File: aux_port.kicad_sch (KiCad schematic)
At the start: 5 parts, among them J1 USB_C

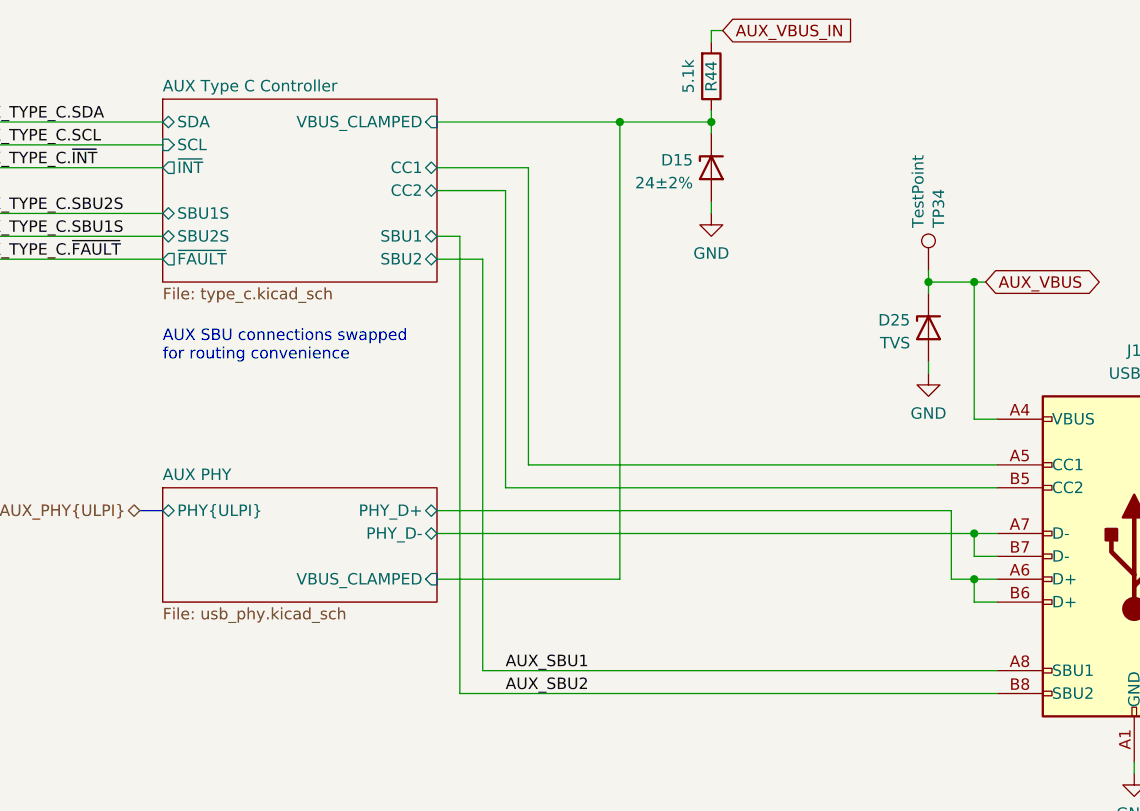
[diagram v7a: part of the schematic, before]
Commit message: Add second common-mode choke for TARGET port
Instead of having a single choke connected in series with the PHY, we
now have a choke in series with each connector. The PHY is connected
between the two chokes.
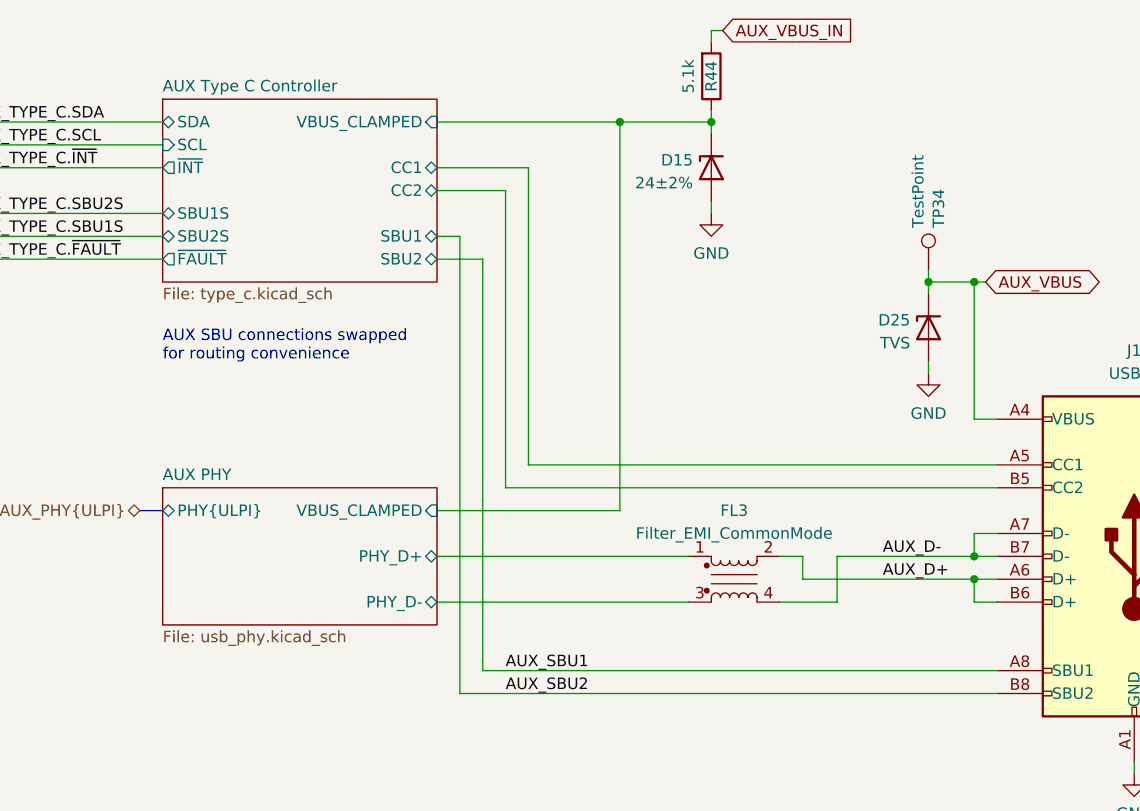
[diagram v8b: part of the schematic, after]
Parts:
- added FL3: Filter_EMI_CommonMode, cynthion:L_CommonModeChoke_Murata_DLM0NS, symbol Device:Filter_EMI_CommonMode
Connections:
- net AUX PHY/PHY_D+: now also FL3.1; no longer J1.A6 (D+), J1.B6 (D+)
- net AUX PHY/PHY_D-: now also FL3.3; no longer J1.A7 (D-), J1.B7 (D-)
- new net AUX_D+: FL3.2, J1.A6 (D+), J1.B6 (D+)
- new net AUX_D-: FL3.4, J1.A7 (D-), J1.B7 (D-)
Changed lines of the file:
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@@
   (junction (at 171.45 59.69) (diameter 0) (color 0 0 0 0)
   )
+  (junction (at 200.66 110.49) (diameter 0) (color 0 0 0 0)
+  )
   (junction (at 161.29 59.69) (diameter 0) (color 0 0 0 0)
   )
@@
   (junction (at 195.58 77.47) (diameter 0) (color 0 0 0 0)
   )
-  (junction (at 200.66 105.41) (diameter 0) (color 0 0 0 0)
-  )
-  (junction (at 200.66 110.49) (diameter 0) (color 0 0 0 0)
+  (junction (at 200.66 107.95) (diameter 0) (color 0 0 0 0)
   )
   (bus_entry (at 83.82 64.77) (size 2.54 -2.54)
@@
     (stroke (width 0) (type default))
   )
+  (wire (pts (xy 140.97 107.95) (xy 168.91 107.95))
+    (stroke (width 0) (type default))
+  )
   (wire (pts (xy 143.51 123.19) (xy 203.2 123.19))
     (stroke (width 0) (type default))
@@
     (stroke (width 0) (type default))
   )
+  (wire (pts (xy 185.42 107.95) (xy 185.42 113.03))
+    (stroke (width 0) (type default))
+  )
   (wire (pts (xy 151.13 64.77) (xy 151.13 97.79))
     (stroke (width 0) (type default))
   )
-  (wire (pts (xy 198.12 102.87) (xy 198.12 110.49))
-    (stroke (width 0) (type default))
-  )
   (wire (pts (xy 151.13 97.79) (xy 203.2 97.79))
     (stroke (width 0) (type default))
   )
+  (wire (pts (xy 185.42 113.03) (xy 179.07 113.03))
+    (stroke (width 0) (type default))
+  )
   (wire (pts (xy 200.66 107.95) (xy 203.2 107.95))
     (stroke (width 0) (type default))
   )
-  (wire (pts (xy 198.12 110.49) (xy 200.66 110.49))
-    (stroke (width 0) (type default))
-  )
   (wire (pts (xy 218.44 130.81) (xy 218.44 132.08))
     (stroke (width 0) (type default))
@@
     (stroke (width 0) (type default))
   )
-  (wire (pts (xy 161.29 110.49) (xy 161.29 59.69))
+  (wire (pts (xy 161.29 102.87) (xy 161.29 59.69))
     (stroke (width 0) (type default))
   )
@@
     (stroke (width 0) (type default))
   )
-  (wire (pts (xy 200.66 105.41) (xy 140.97 105.41))
+  (wire (pts (xy 181.61 107.95) (xy 181.61 110.49))
     (stroke (width 0) (type default))
   )
@@
     (stroke (width 0) (type default))
   )
-  (wire (pts (xy 161.29 110.49) (xy 140.97 110.49))
-    (stroke (width 0) (type default))
-  )
   (wire (pts (xy 143.51 72.39) (xy 143.51 123.19))
     (stroke (width 0) (type default))
@@
     (stroke (width 0) (type default))
   )
+  (wire (pts (xy 200.66 107.95) (xy 185.42 107.95))
+    (stroke (width 0) (type default))
+  )
   (wire (pts (xy 203.2 92.71) (xy 200.66 92.71))
     (stroke (width 0) (type default))
@@
     (stroke (width 0) (type default))
   )
+  (wire (pts (xy 140.97 102.87) (xy 161.29 102.87))
+    (stroke (width 0) (type default))
+  )
   (bus (pts (xy 83.82 74.93) (xy 83.82 72.39))
     (stroke (width 0) (type default))
@@
     (stroke (width 0) (type default))
   )
-  (wire (pts (xy 140.97 102.87) (xy 198.12 102.87))
+  (wire (pts (xy 181.61 110.49) (xy 200.66 110.49))
     (stroke (width 0) (type default))
   )
@@
   )
   (wire (pts (xy 140.97 67.31) (xy 148.59 67.31))
+    (stroke (width 0) (type default))
+  )
+  (wire (pts (xy 140.97 113.03) (xy 168.91 113.03))
+    (stroke (width 0) (type default))
+  )
+  (wire (pts (xy 179.07 107.95) (xy 181.61 107.95))
     (stroke (width 0) (type default))
   )
@@
     (effects (font (size 1.27 1.27)) (justify left bottom))
   )
+  (label "AUX_D+" (at 190.5 110.49 0) (fields_autoplaced)
+    (effects (font (size 1.27 1.27)) (justify left bottom))
+  )
   (label "AUX_TYPE_C.SBU2S" (at 88.9 69.85 0) (fields_autoplaced)
     (effects (font (size 1.27 1.27)) (justify left bottom))
@@
   )
   (label "AUX_TYPE_C.SCL" (at 88.9 62.23 0) (fields_autoplaced)
+    (effects (font (size 1.27 1.27)) (justify left bottom))
+  )
+  (label "AUX_D-" (at 190.5 107.95 0) (fields_autoplaced)
     (effects (font (size 1.27 1.27)) (justify left bottom))
   )
@@
     )
   )
+  (symbol (lib_id "Device:Filter_EMI_CommonMode") (at 173.99 110.49 0) (unit 1)
+    (in_bom yes) (on_board yes) (dnp no)
+    (property "Reference" "FL3" (at 173.99 102.87 0)
+      (effects (font (size 1.27 1.27)))
+    )
+    (property "Value" "Filter_EMI_CommonMode" (at 173.99 105.4069 0)
+      (effects (font (size 1.27 1.27)))
+    )
+    (property "Footprint" "cynthion:L_CommonModeChoke_Murata_DLM0NS" (at 173.99 109.474 0)
+      (effects (font (size 1.27 1.27)) hide)
+    )
+    (property "Datasheet" "https://www.murata.com/en-global/products/productdata/8799424610334/EFLD0009.pdf" (at 173.99 109.474 0)
+      (effects (font (size 1.27 1.27)) hide)
+    )
+    (property "Description" "CMC 130MA 2LN 28 OHM SMD" (at 173.99 110.49 0)
+      (effects (font (size 1.27 1.27)) hide)
+    )
+    (property "Manufacturer" "Murata" (at 173.99 110.49 0)
+      (effects (font (size 1.27 1.27)) hide)
+    )
+    (property "Part Number" "DLM0NSB280HY2D" (at 173.99 110.49 0)
+      (effects (font (size 1.27 1.27)) hide)
+    )
+    (pin "1")
+    (pin "2")
+    (pin "3")
+    (pin "4")
+    (instances
+      (project "cynthion"
+        (path "/fb621148-8145-4217-9712-738e1b5a4823/00000000-0000-0000-0000-00005dcd9772/86be2f0e-7bb1-42d8-87bc-4230c6dbd013"
+          (reference "FL3") (unit 1)
+        )
+        (path "/fb621148-8145-4217-9712-738e1b5a4823/00000000-0000-0000-0000-00005dd754d4/6ef06f1e-62a2-438c-8ab4-363586d03e74"
+          (reference "FL1") (unit 1)
+        )
+        (path "/fb621148-8145-4217-9712-738e1b5a4823/00000000-0000-0000-0000-00005dddb747/6fe66c21-f87e-45b5-9c98-390633af1111"
+          (reference "FL2") (unit 1)
+        )
+        (path "/fb621148-8145-4217-9712-738e1b5a4823/00000000-0000-0000-0000-00005dd754d4"
+          (reference "FL1") (unit 1)
+        )
+      )
+    )
+  )
   (symbol (lib_id "power:GND") (at 195.58 87.63 0) (unit 1)
     (in_bom yes) (on_board yes) (dnp no) (fields_autoplaced)
@@
     )
   )
-  (sheet (at 110.49 100.33) (size 30.48 12.7) (fields_autoplaced)
+  (sheet (at 110.49 100.33) (size 30.48 15.24) (fields_autoplaced)
     (stroke (width 0.1524) (type solid))
     (fill (color 0 0 0 0.0000))
@@
       (effects (font (size 1.27 1.27)) (justify left bottom))
     )
-    (property "Sheetfile" "usb_phy.kicad_sch" (at 110.49 113.6146 0)
+    (property "Sheetfile" "usb_phy.kicad_sch" (at 110.49 116.1546 0)
       (effects (font (size 1.27 1.27)) (justify left top))
     )
-    (pin "PHY_D-" bidirectional (at 140.97 105.41 0)
+    (pin "PHY_D-" bidirectional (at 140.97 113.03 0)
       (effects (font (size 1.27 1.27)) (justify right))
     )
-    (pin "PHY_D+" bidirectional (at 140.97 102.87 0)
+    (pin "PHY_D+" bidirectional (at 140.97 107.95 0)
       (effects (font (size 1.27 1.27)) (justify right))
     )
@@
       (effects (font (size 1.27 1.27)) (justify left))
     )
-    (pin "VBUS_CLAMPED" input (at 140.97 110.49 0)
+    (pin "VBUS_CLAMPED" input (at 140.97 102.87 0)
       (effects (font (size 1.27 1.27)) (justify right))
     )
